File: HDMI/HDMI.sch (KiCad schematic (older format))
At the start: 15 parts, among them J1 HDMI, J2 PMOD, U1 NCP1402SN33T1G

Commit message: Changing schematic tu use bidirectional pins
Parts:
- removed J2: PMOD, Connector_PinHeader_2.54mm:PinHeader_2x06_P2.54mm_Horizontal, symbol Connector_Generic:Conn_02x06_Odd_Even
- added C? (x2): 220nF, Capacitor_SMD:C_0603_1608Metric, symbol Device:C
- added C?: 470pF, symbol Device:C
- added J?: PMOD, symbol Connector_Generic:Conn_02x09_Odd_Even
- added R?: 510, symbol Device:R
- added R?: 100k, symbol Device:R
- added R? (x2): 4.7k, symbol Device:R
- added R? (x2): 3.3k, symbol Device:R
- added U?: PCA9306, symbol Interface:PCA9306
- U1: symbol NCP1402SN33T1G:NCP1402SN33T1G -> HDMI-rescue:NCP1402SN33T1G-NCP1402SN33T1G
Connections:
- net labels added: GPDI_CEC, GPDI_ETH+, GPDI_ETH-, GPDI_SCL, GPDI_SDA, LED_HDMI, PMOD_SCL, PMOD_SDA
- net labels removed: FPDI_CLK+, FPDI_CLK-, FPDI_D0+, FPDI_D0-, FPDI_D1+, FPDI_D1-, FPDI_D2+, FPDI_D2-
- wire segments 54 -> 98
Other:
- note added: "GP13 ETH+\nGN13 ETH-\nGP12 CLK+\nGN12 CLK-\nGP11 D2+\nGN11 D2-\nGP10 D1+\nGN10 D1-\nGP9 D0+\nGN9 D0-\nGP8 SDA over i2c chip\nGN8 SCL over i2c chip\nGP7 CEC over 510 ohm resistor\nGN7 onboard LED"
- note added: "Negative - Positive"
- moved on the sheet: C1, C11, C12, C2, C3, C4, C6, C7, C8, C9, D1, L1

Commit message: Changing HDMI connector -- initial placement
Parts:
- removed J1: HDMI, hdmi-swm-19:hdmi-swm-19, symbol Connector_Generic:Conn_01x20
- added D2: LED, LED_SMD:LED_0603_1608Metric_Pad1.05x0.95mm_HandSolder, symbol Device:LED
- added P?: HDMI-D, symbol hdmi-d:HDMI-D
- added R2: 4.7k, Resistor_SMD:R_0603_1608Metric_Pad1.05x0.95mm_HandSolder, symbol Device:R
- C1, C2, C3, C4, C6, C7, C8, C9: footprint Capacitor_SMD:C_0603_1608Metric -> Capacitor_SMD:C_0603_1608Metric_Pad1.05x0.95mm_HandSolder
- C10, C5: renamed from C?; footprint Capacitor_SMD:C_0603_1608Metric -> Capacitor_SMD:C_0603_1608Metric_Pad1.05x0.95mm_HandSolder
- C11, C12: footprint Capacitor_Tantalum_SMD:CP_EIA-1608-08_AVX-J_Pad1.25x1.05mm_HandSolder -> Capacitor_Tantalum_SMD:CP_EIA-7343-15_Kemet-W_Pad2.25x2.55mm_HandSolder
- C13: renamed from C?; footprint (none) -> Capacitor_SMD:C_0603_1608Metric_Pad1.05x0.95mm_HandSolder
- J2: renamed from J?; footprint (none) -> Connector_PinHeader_2.54mm:PinHeader_2x09_P2.54mm_Horizontal
- L1: footprint Inductor_SMD:L_6.3x6.3_H3 -> Inductor_SMD:L_1210_3225Metric_Pad1.42x2.65mm_HandSolder
- R1, R3, R4, R5, R6, R7: renamed from R?; footprint (none) -> Resistor_SMD:R_0603_1608Metric_Pad1.05x0.95mm_HandSolder
- U2: renamed from U?; footprint (none) -> Package_SO:SSOP-8_2.95x2.8mm_P0.65mm
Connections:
- wire segments 98 -> 102

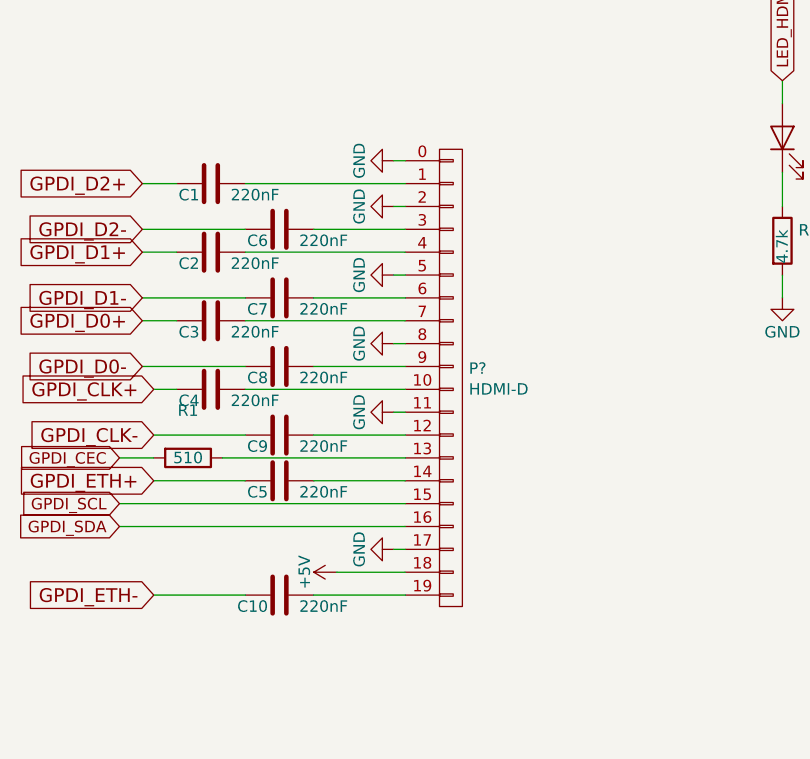
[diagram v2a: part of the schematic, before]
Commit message: Finished routing HDMI INPUt
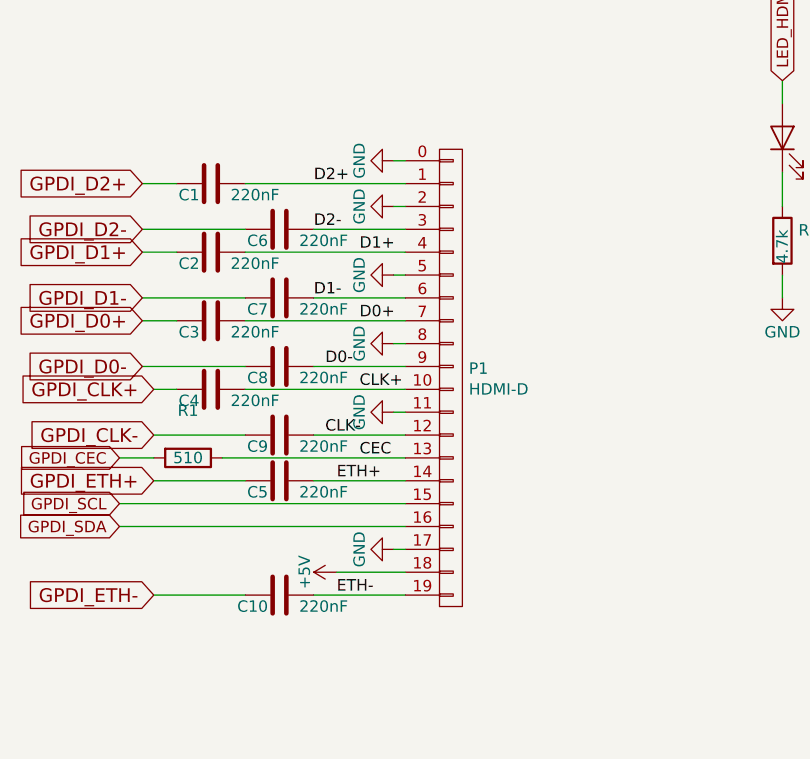
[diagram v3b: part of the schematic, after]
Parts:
- P1: renamed from P?; footprint (none) -> HDMI:HDMI-D
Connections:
- net CLK+: now reaches C4.2, P1.10 (P10)
- net CLK-: now reaches C9.2, P1.12 (P12)
- net D0-: now reaches C8.2, P1.9 (P9)
- net D0+: now reaches C3.2, P1.7 (P7)
- net D1-: now reaches C7.2, P1.6 (P6)
- net D1+: now reaches C2.2, P1.4 (P4)
- net D2+: now reaches C1.2, P1.1 (P1)
- net D2-: now reaches C6.2, P1.3 (P3)
- net CEC: now reaches P1.13 (P13), R1.1
- net ETH+: now reaches C5.2, P1.14 (P14)
- net ETH-: now reaches C10.2, P1.19 (P19)
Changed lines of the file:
@@
 	3750 4000 3800 4000
 $Comp
-L hdmi-d:HDMI-D P?
+L hdmi-d:HDMI-D P1
 U 1 1 5DF81DAE
 P 4000 4150
-F 0 "P?" H 4078 4191 50  0000 L CNN
+F 0 "P1" H 4078 4191 50  0000 L CNN
 F 1 "HDMI-D" H 4078 4100 50  0000 L CNN
-F 2 "" H 4000 4150 60  0000 C CNN
+F 2 "HDMI:HDMI-D" H 4000 4150 60  0001 C CNN
 F 3 "" H 4000 4150 60  0000 C CNN
 	1    4000 4150
 	1    0    0    -1
 $EndComp
+Text Label 3400 3300 0    50   ~ 0
+D2+
+Text Label 3400 3500 0    50   ~ 0
+D2-
+Text Label 3600 3600 0    50   ~ 0
+D1+
+Text Label 3400 3800 0    50   ~ 0
+D1-
+Text Label 3600 3900 0    50   ~ 0
+D0+
+Text Label 3450 4100 0    50   ~ 0
+D0-
+Text Label 3600 4200 0    50   ~ 0
+CLK+
+Text Label 3500 4600 0    50   ~ 0
+ETH+
+Text Label 3500 5100 0    50   ~ 0
+ETH-
+Text Label 3600 4500 0    50   ~ 0
+CEC
+Text Label 3450 4400 0    50   ~ 0
+CLK-
 $EndSCHEMATC

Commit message: Adding screws - adding OSH Park logos
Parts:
- C11, C12: footprint Capacitor_Tantalum_SMD:CP_EIA-7343-15_Kemet-W_Pad2.25x2.55mm_HandSolder -> Capacitor_Tantalum_SMD:CP_EIA-3216-10_Kemet-I
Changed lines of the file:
@@
 F 0 "C12" H 8368 4796 50  0000 L CNN
 F 1 "CP" H 8368 4705 50  0000 L CNN
-F 2 "Capacitor_Tantalum_SMD:CP_EIA-7343-15_Kemet-W_Pad2.25x2.55mm_HandSolder" H 8288 4600 50  0001 C CNN
+F 2 "Capacitor_Tantalum_SMD:CP_EIA-3216-10_Kemet-I" H 8288 4600 50  0001 C CNN
 F 3 "~" H 8250 4750 50  0001 C CNN
 	1    8250 4750
@@
 F 0 "C11" H 6368 4746 50  0000 L CNN
 F 1 "CP" H 6368 4655 50  0000 L CNN
-F 2 "Capacitor_Tantalum_SMD:CP_EIA-7343-15_Kemet-W_Pad2.25x2.55mm_HandSolder" H 6288 4550 50  0001 C CNN
+F 2 "Capacitor_Tantalum_SMD:CP_EIA-3216-10_Kemet-I" H 6288 4550 50  0001 C CNN
 F 3 "~" H 6250 4700 50  0001 C CNN
 	1    6250 4700

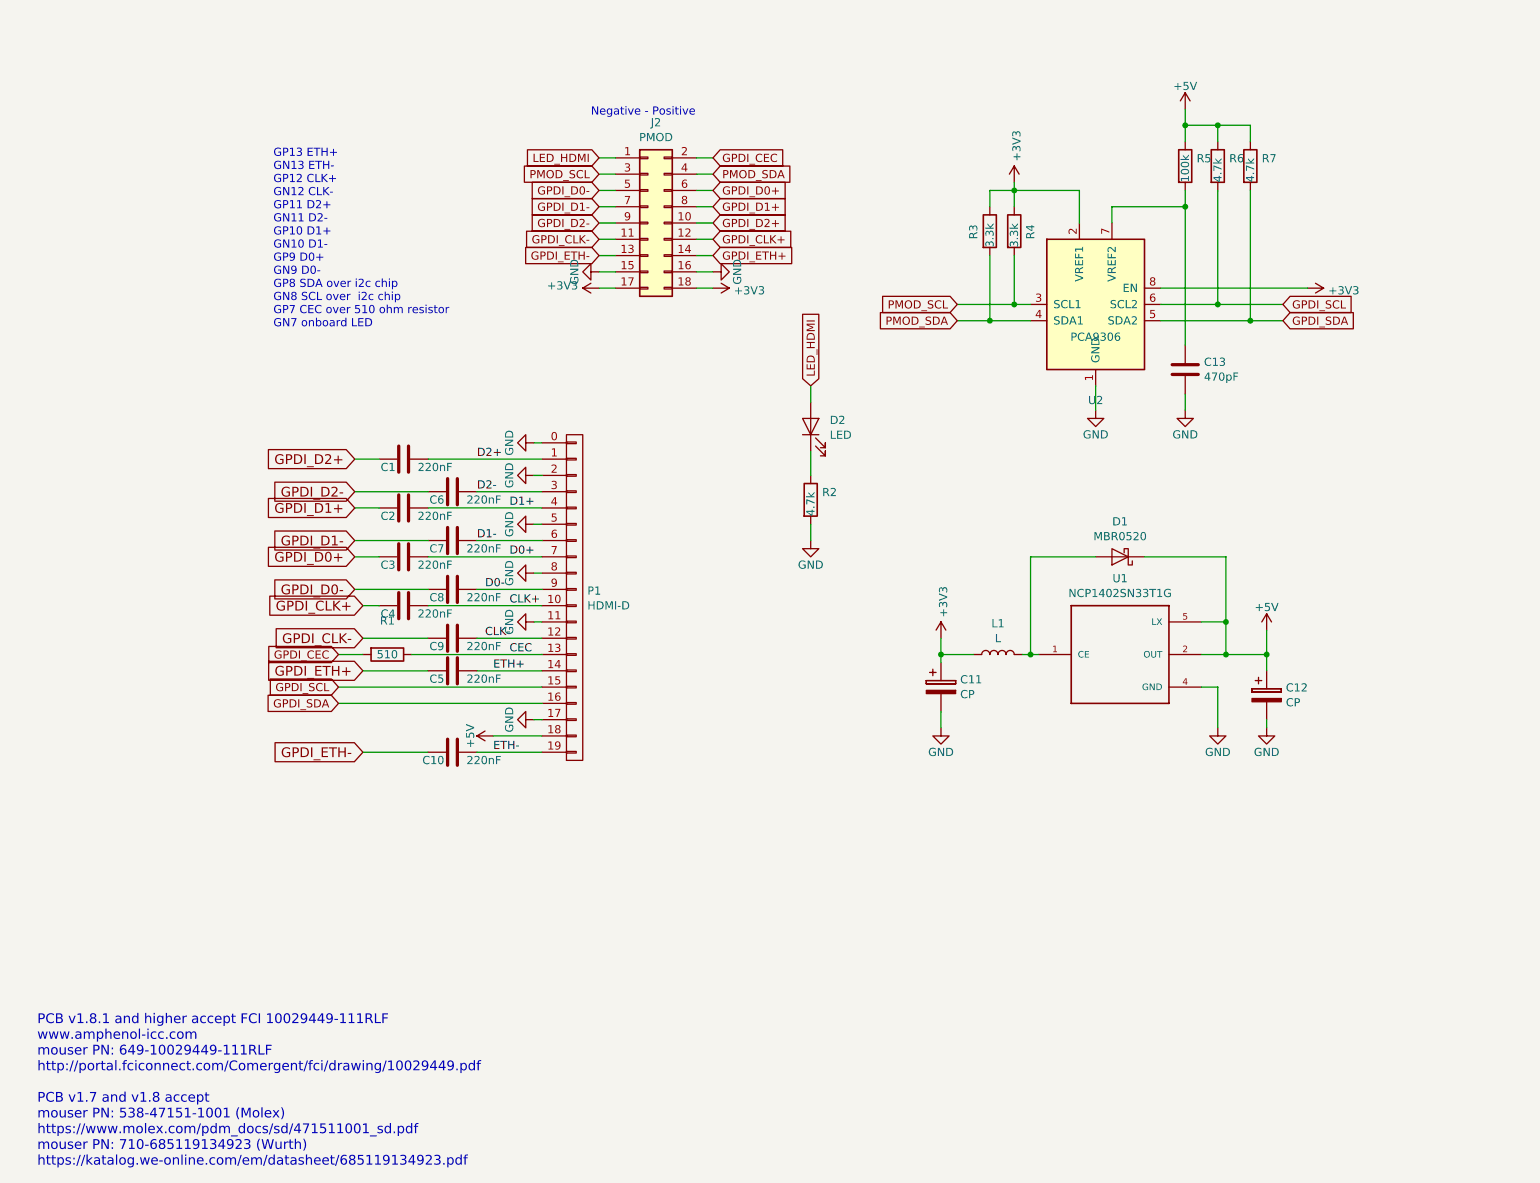
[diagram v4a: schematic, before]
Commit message: Adding pullups for HDMI input
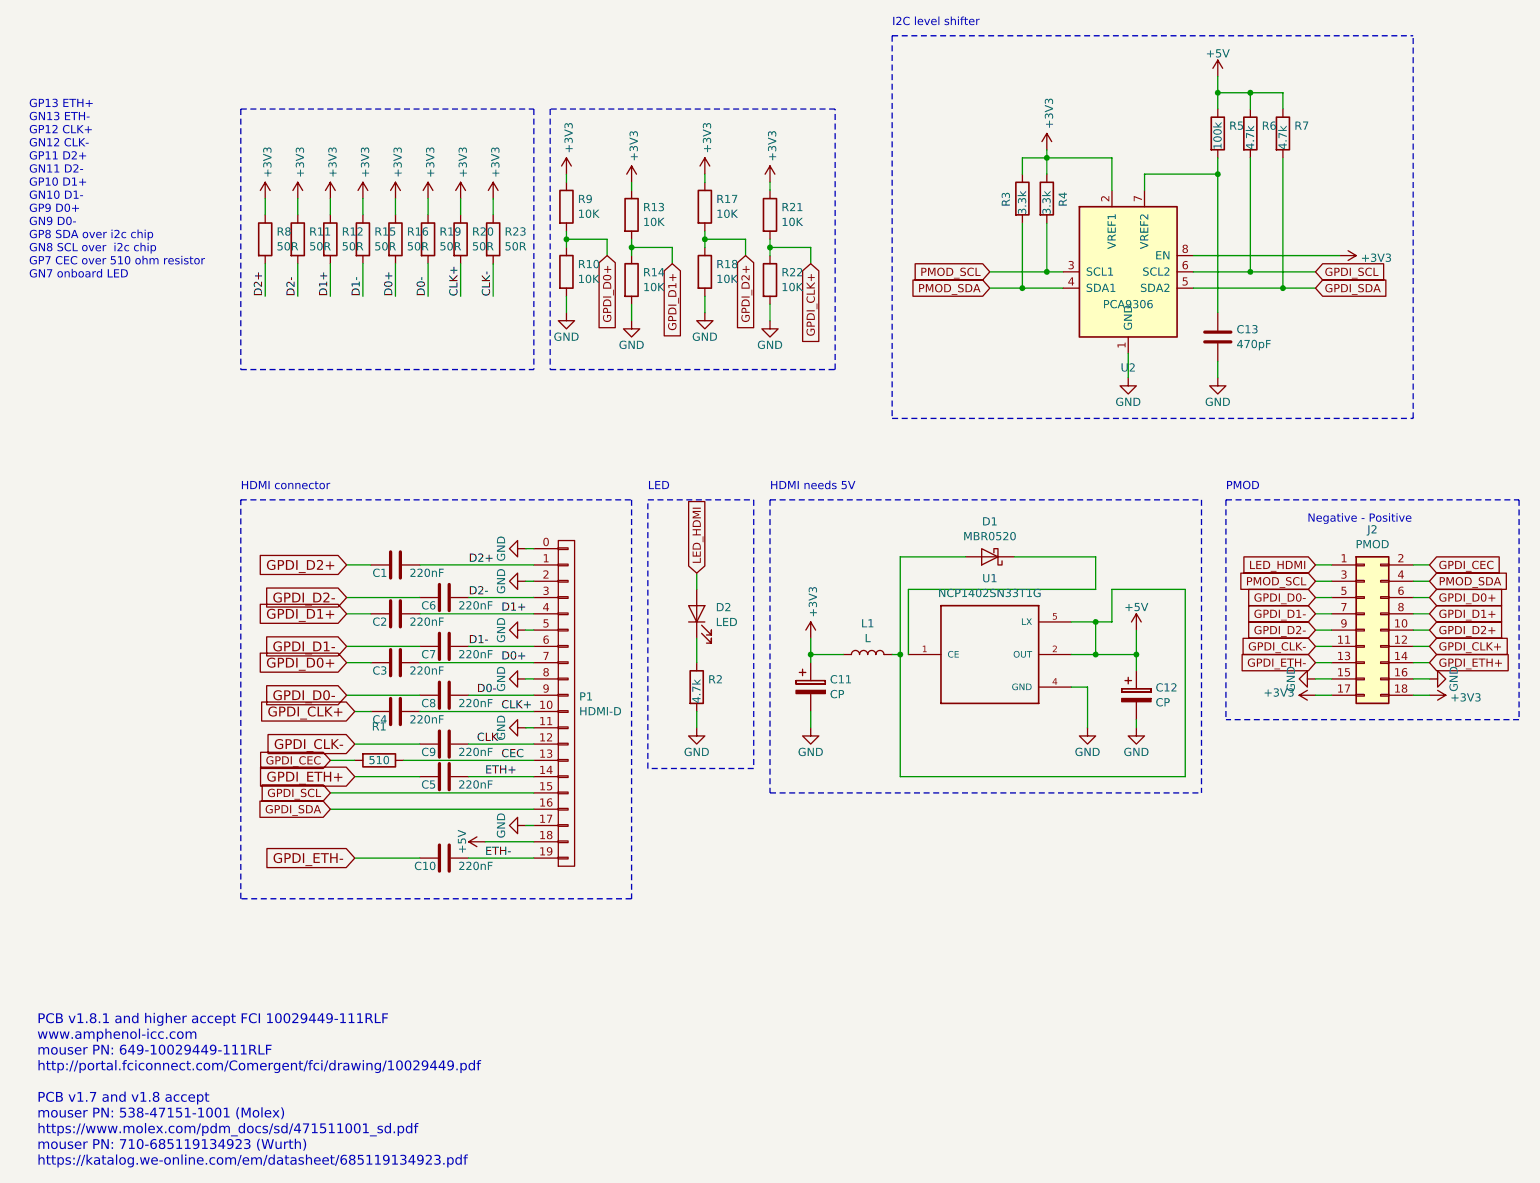
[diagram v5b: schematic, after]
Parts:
- added R10, R13, R14, R17, R18, R21, R22, R9: 10K, Resistor_SMD:R_0603_1608Metric_Pad1.05x0.95mm_HandSolder, symbol antena:R
- added R11, R12, R15, R16, R19, R20, R23, R8: 50R, Resistor_SMD:R_0603_1608Metric_Pad1.05x0.95mm_HandSolder, symbol antena:R
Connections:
- net +3V3: now also R11.1, R12.1, R13.1, R15.1, R16.1, R17.1, R19.1, R20.1, R21.1, R23.1, R8.1, R9.1
- net +5V: now also D1.2 (A), L1.2; no longer D1.1 (K)
- net CLK+: now also R20.2
- net CLK-: now also R23.2
- net D0+: now also R16.2
- net D0-: now also R19.2
- net D1+: now also R12.2
- net D1-: now also R15.2
- net D2+: now also R8.2
- net D2-: now also R11.2
- net GND: now also R10.2, R14.2, R18.2, R22.2
- net GPDI_CLK+: now also R21.2, R22.1
- net GPDI_D0+: now also R10.1, R9.2
- net GPDI_D1+: now also R13.2, R14.1
- net GPDI_D2+: now also R17.2, R18.1
- new net: D1.1 (K), U1.1 (CE)
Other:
- note added: "HDMI connector"
- note added: "HDMI needs 5V"
- note added: "I2C level shifter"
- note added: "LED"
- note added: "PMOD"
- moved on the sheet: C1, C10, C11, C12, C13, C2, C3, C4, C5, C6, C7, C8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
